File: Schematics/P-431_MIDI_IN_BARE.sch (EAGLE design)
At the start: 19 parts, among them X1 MIDI IN, X4 CTRL OUT and POWER

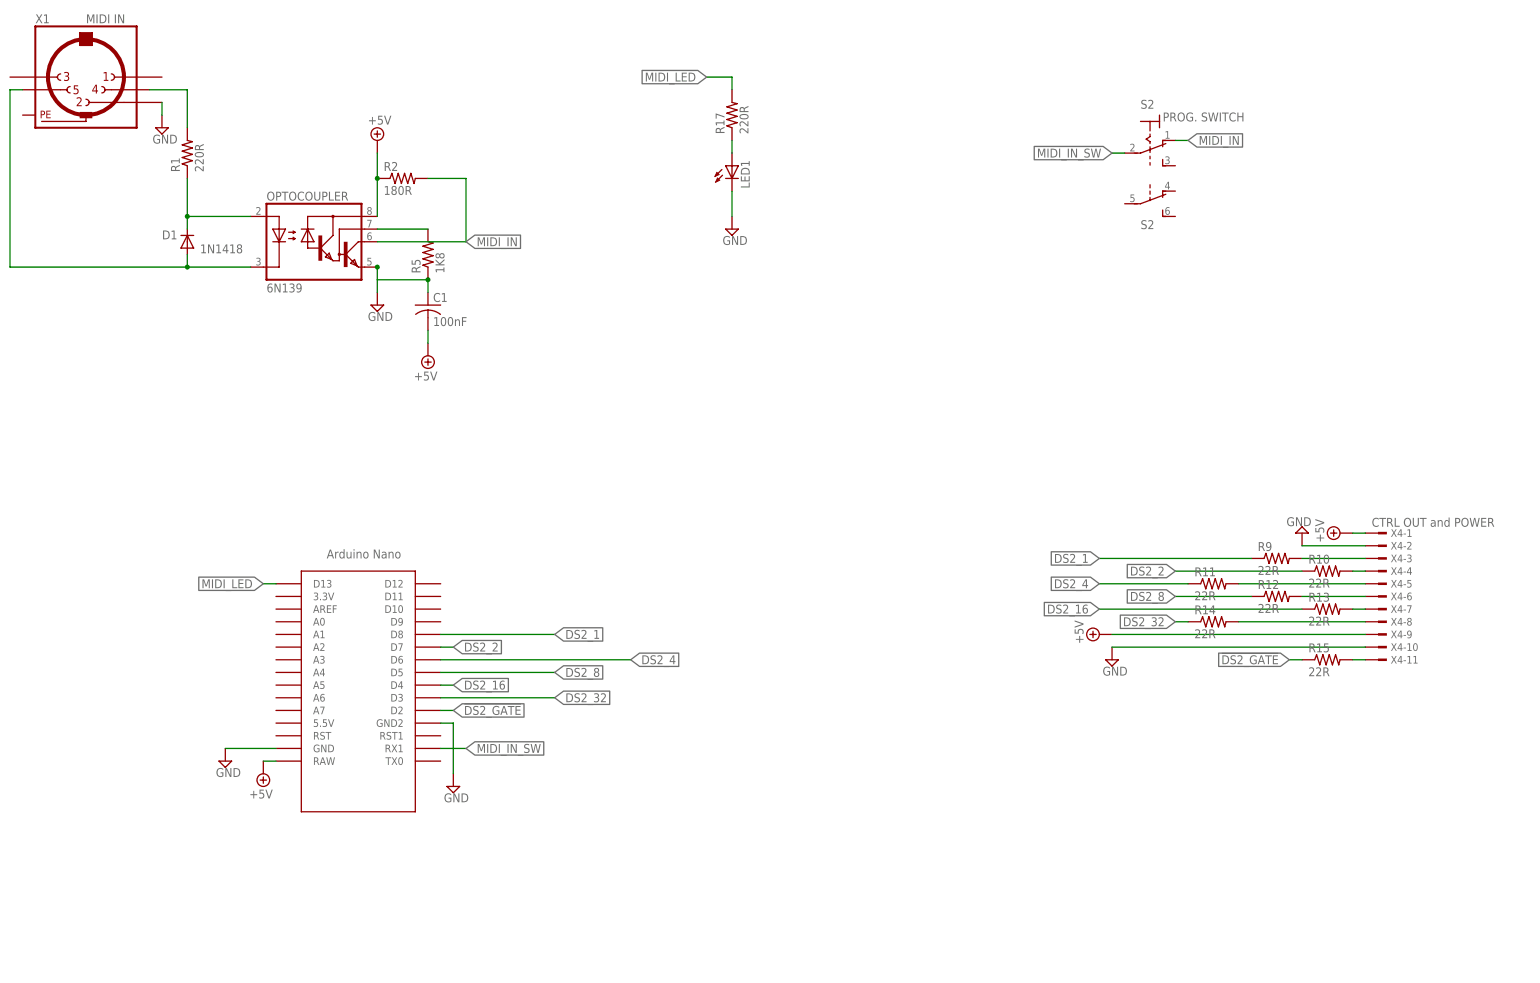
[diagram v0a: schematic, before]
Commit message: Added reset pullup resistor and fixed resistors value for optocoupler
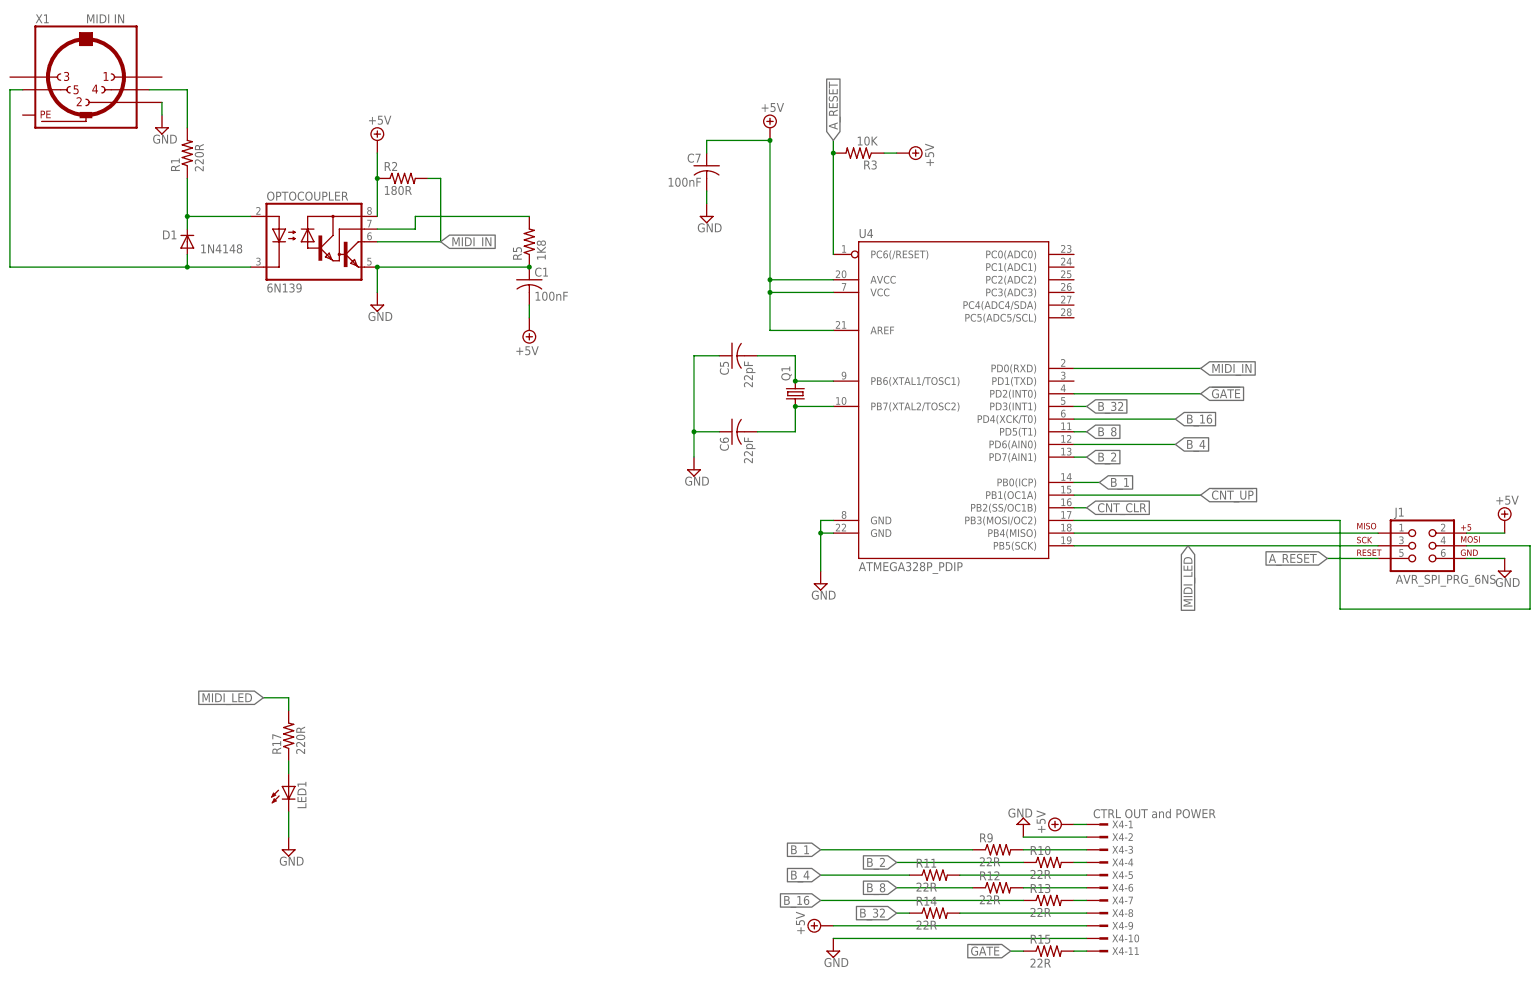
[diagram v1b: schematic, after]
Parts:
- removed S2: PROG. SWITCH, switch:320-938
- removed U$1: NANO, Arduino-clone:NANO
- added C5, C6: 22pF, rcl:C-US050-025X075
- added C7: 100nF, rcl:C-US050-025X075
- added J1: AVR_SPI_PRG_6NS, SparkFun:AVR_SPI_PRG_6NS
- added Q1: (no value), crystal:CRYSTALHC49S
- added R3: 10K, resistor:R-US_0207/7
- added U4: ATMEGA328P_PDIP, SparkFun-DigitalIC:ATMEGA328P_PDIP
- D1: value 1N1418 -> 1N4148
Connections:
- removed net !DS2_GATE: R15.1, U$1.D2
- removed net DS2_1: R9.1, U$1.D8
- removed net DS2_16: R13.1, U$1.D4
- removed net DS2_2: R10.1, U$1.D7
- removed net DS2_32: R14.1, U$1.D3
- removed net DS2_4: R11.1, U$1.D6
- removed net DS2_8: R12.1, U$1.D5
- removed net MIDI_IN_SW: S21.P, U$1.RX1
- new net !CNT_UP: U4.PB1(OC1A)
- new net !GATE: R15.1, U4.PD2(INT0)
- new net A_RESET: J1.5, R3.2, U4.PC6(/RESET)
- new net B_1: R9.1, U4.PB0(ICP)
- new net B_16: R13.1, U4.PD4(XCK/T0)
- new net B_2: R10.1, U4.PD7(AIN1)
- new net B_32: R14.1, U4.PD3(INT1)
- new net B_4: R11.1, U4.PD6(AIN0)
- new net B_8: R12.1, U4.PD5(T1)
- new net CNT_CLR: U4.PB2(SS/OC1B)
- new net N$26: C5.2, Q1.2, U4.PB6(XTAL1/TOSC1)
- new net N$27: C6.2, Q1.1, U4.PB7(XTAL2/TOSC2)
- new net POT_DI: J1.1, U4.PB4(MISO)
- new net POT_SCK: J1.4, U4.PB3(MOSI/OC2)
- net +5V: now also C7.1, J1.2, R3.1, U4.AREF, U4.AVCC, U4.VCC; no longer U$1.RAW
- net GND: now also C5.1, C6.1, C7.2, J1.6, U4.GND@1, U4.GND@2; no longer U$1.GND, U$1.GND2
- net MIDI_IN: now also U4.PD0(RXD); no longer S21.O
- net MIDI_LED: now also J1.3, U4.PB5(SCK); no longer U$1.D13
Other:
- moved on the sheet: C1, LED1, R10, R11, R12, R13, R14, R15, R17, R5, R9, X4-1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
